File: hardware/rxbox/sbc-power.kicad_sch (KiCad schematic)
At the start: 41 parts, among them U2 SY8088, U3 SY8088, U4 SY8088, U5 SY8088, U6 ME6211C18M5, U7 SY8088

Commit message: supervisor + symbol, new journal. jumper for t113 power
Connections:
- net +5V renamed T113_5V
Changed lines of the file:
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@@
 		(in_pos_files yes)
 		(dnp no)
-		(fields_autoplaced yes)
 		(property "Reference" "#PWR07"
 			(at 52.07 91.44 0)
@@
 			)
 		)
-		(property "Value" "+5V"
-			(at 52.07 82.55 0)
+		(property "Value" "T113_5V"
+			(at 48.26 83.312 0)
 			(show_name no)
 			(do_not_autoplace no)
@@
 					(size 1.27 1.27)
 				)
+				(justify left)
 			)
 		)
@@
 		(in_pos_files yes)
 		(dnp no)
-		(fields_autoplaced yes)
 		(property "Reference" "#PWR016"
 			(at 140.97 91.44 0)
@@
 			)
 		)
-		(property "Value" "+5V"
-			(at 140.97 82.55 0)
+		(property "Value" "T113_5V"
+			(at 137.16 83.312 0)
 			(show_name no)
 			(do_not_autoplace no)
@@
 					(size 1.27 1.27)
 				)
+				(justify left)
 			)
 		)
@@
 		(in_pos_files yes)
 		(dnp no)
-		(fields_autoplaced yes)
 		(property "Reference" "#PWR02"
 			(at 53.34 50.8 0)
@@
 			)
 		)
-		(property "Value" "+5V"
-			(at 53.34 41.91 0)
+		(property "Value" "T113_5V"
+			(at 49.53 42.672 0)
 			(show_name no)
 			(do_not_autoplace no)
@@
 					(size 1.27 1.27)
 				)
+				(justify left)
 			)
 		)
@@
 			)
 		)
-		(property "Value" "+5V"
+		(property "Value" "T113_5V"
 			(at 52.07 123.19 0)
 			(show_name no)
@@
 		(in_pos_files yes)
 		(dnp no)
-		(fields_autoplaced yes)
 		(property "Reference" "#PWR03"
 			(at 143.51 46.99 0)
@@
 			)
 		)
-		(property "Value" "+5V"
-			(at 143.51 38.1 0)
+		(property "Value" "T113_5V"
+			(at 139.7 38.862 0)
 			(show_name no)
 			(do_not_autoplace no)
@@
 					(size 1.27 1.27)
 				)
+				(justify left)
 			)
 		)
@@
 			)
 		)
-		(property "Value" "+5V"
+		(property "Value" "T113_5V"
 			(at 226.06 82.55 0)
 			(show_name no)

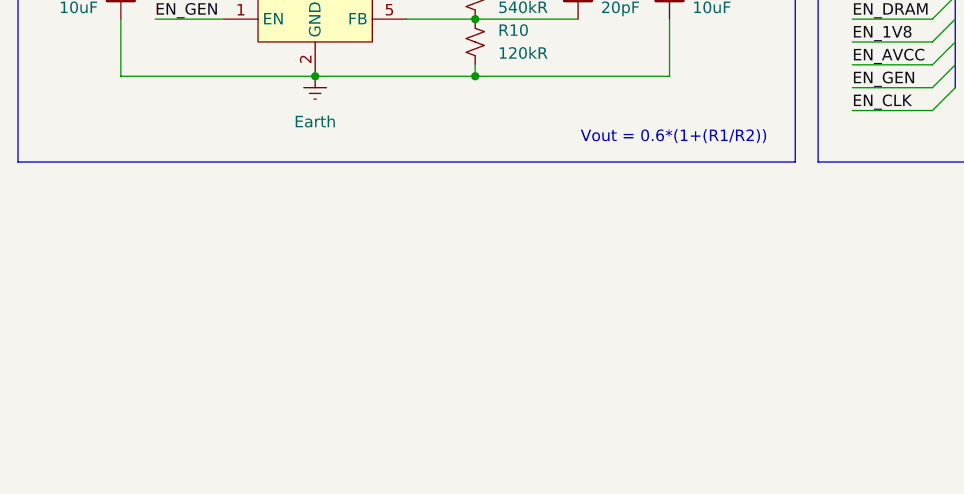
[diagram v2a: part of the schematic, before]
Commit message: wifi updates
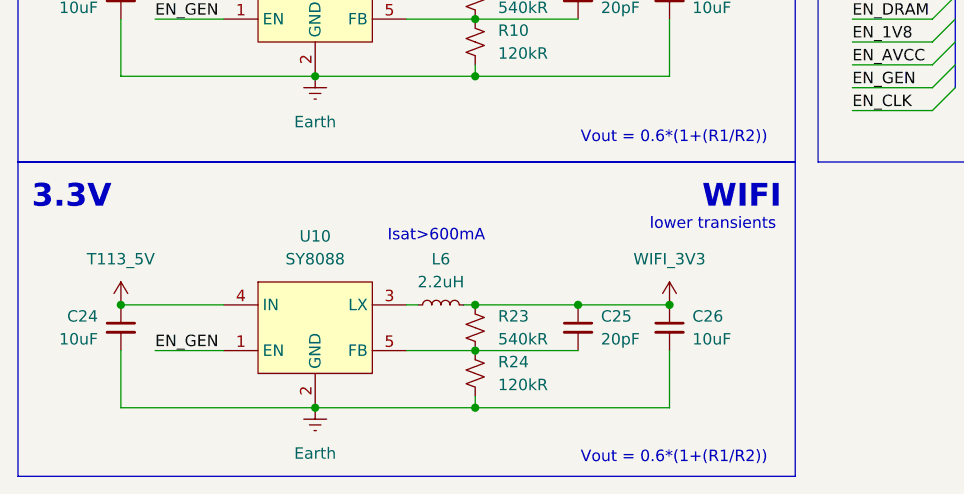
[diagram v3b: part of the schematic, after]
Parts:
- added C24, C26: 10uF, Capacitor_SMD:C_0402_1005Metric, symbol Device:C_Small
- added C25: 20pF, Capacitor_SMD:C_0402_1005Metric, symbol Device:C_Small
- added L6: 2.2uH, symbol Device:L_Small
- added R23: 540kR, Resistor_SMD:R_0402_1005Metric, symbol Device:R_Small_US
- added R24: 120kR, Resistor_SMD:R_0402_1005Metric, symbol Device:R_Small_US
- added U10: SY8088, Package_TO_SOT_SMD:SOT-23-5, symbol Regulator_Custom:SY8088
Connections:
- net EN_GEN: now also U10.1 (EN)
- net Earth: now also C24.2, C26.2, R24.2, U10.2 (GND)
- net T113_5V: now also C24.1, U10.4 (IN)
- new net: C25.2, R23.2, R24.1, U10.5 (FB)
- new net: L6.1, U10.3 (LX)
- new net WIFI_3V3: C25.1, C26.1, L6.2, R23.1
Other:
- note added: "WIFI"
- note added: "lower transients"

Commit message: wiring wifi + bt to t113
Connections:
- net T113_5V: no longer C24.1, U10.4 (IN)
- new net WIFI_5V: C24.1, U10.4 (IN)
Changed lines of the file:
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@@
 		(in_pos_files yes)
 		(dnp no)
-		(fields_autoplaced yes)
 		(property "Reference" "#PWR050"
 			(at 52.07 168.91 0)
@@
 			)
 		)
-		(property "Value" "T113_5V"
-			(at 52.07 160.02 0)
+		(property "Value" "WIFI_5V"
+			(at 53.34 163.83 0)
 			(show_name no)
 			(do_not_autoplace no)
@@
 					(size 1.27 1.27)
 				)
+				(justify left)
 			)
 		)

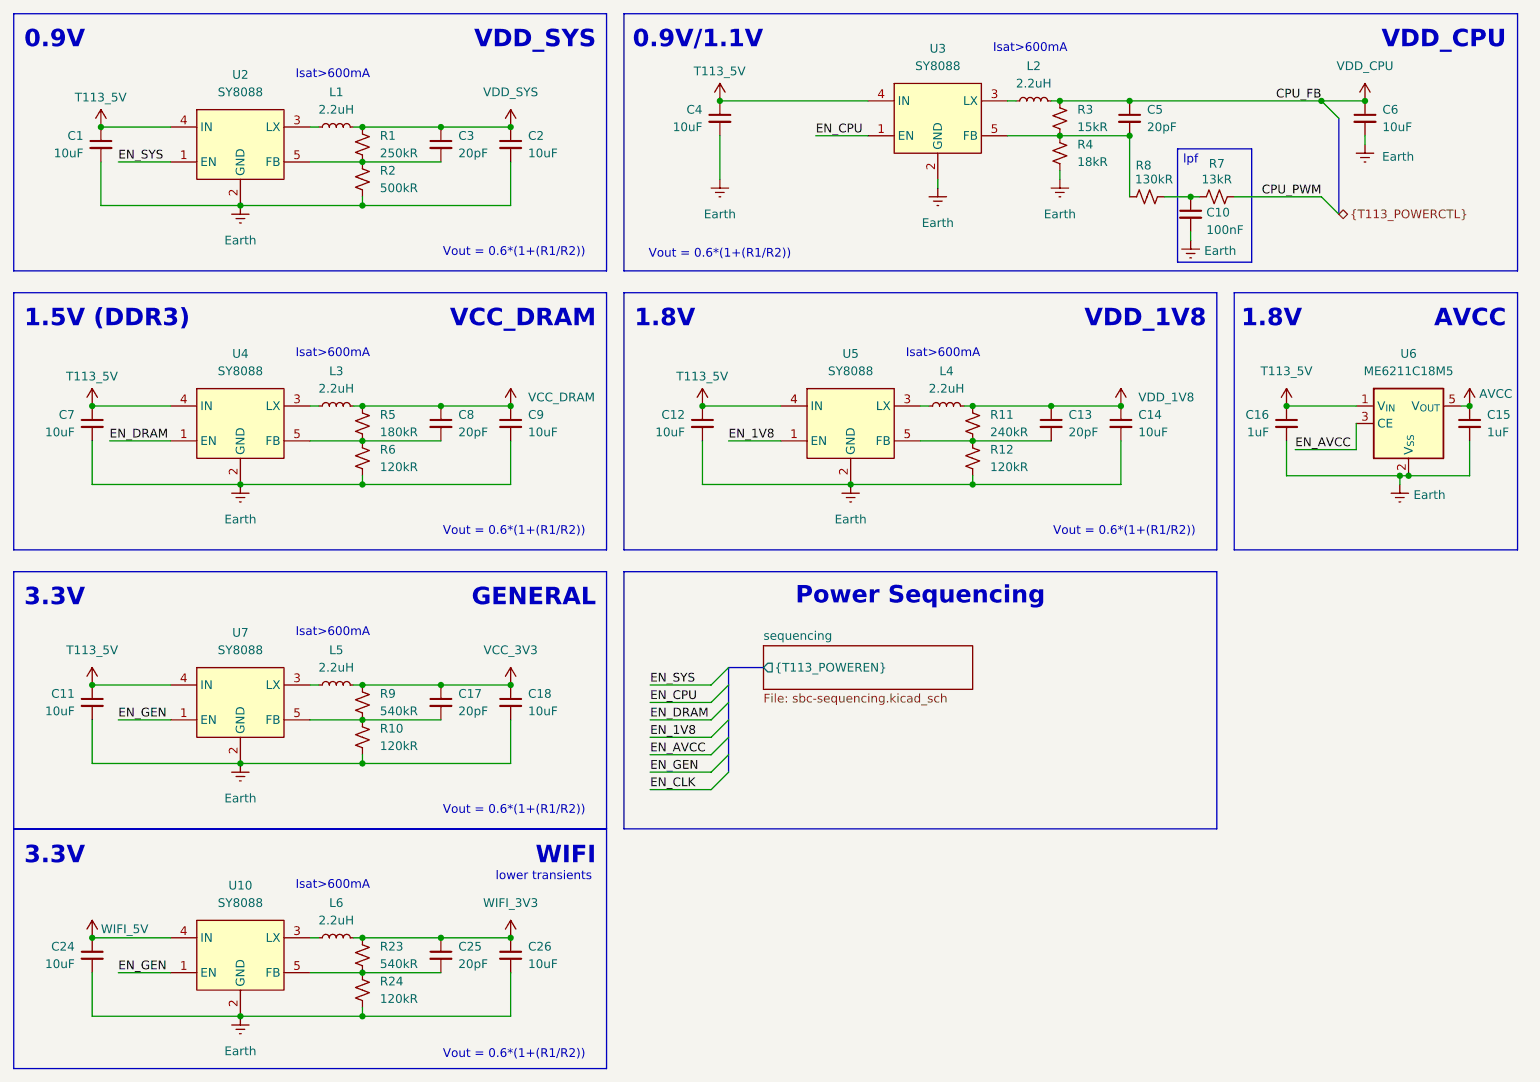
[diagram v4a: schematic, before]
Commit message: finish hooking up wifi+bt, and power
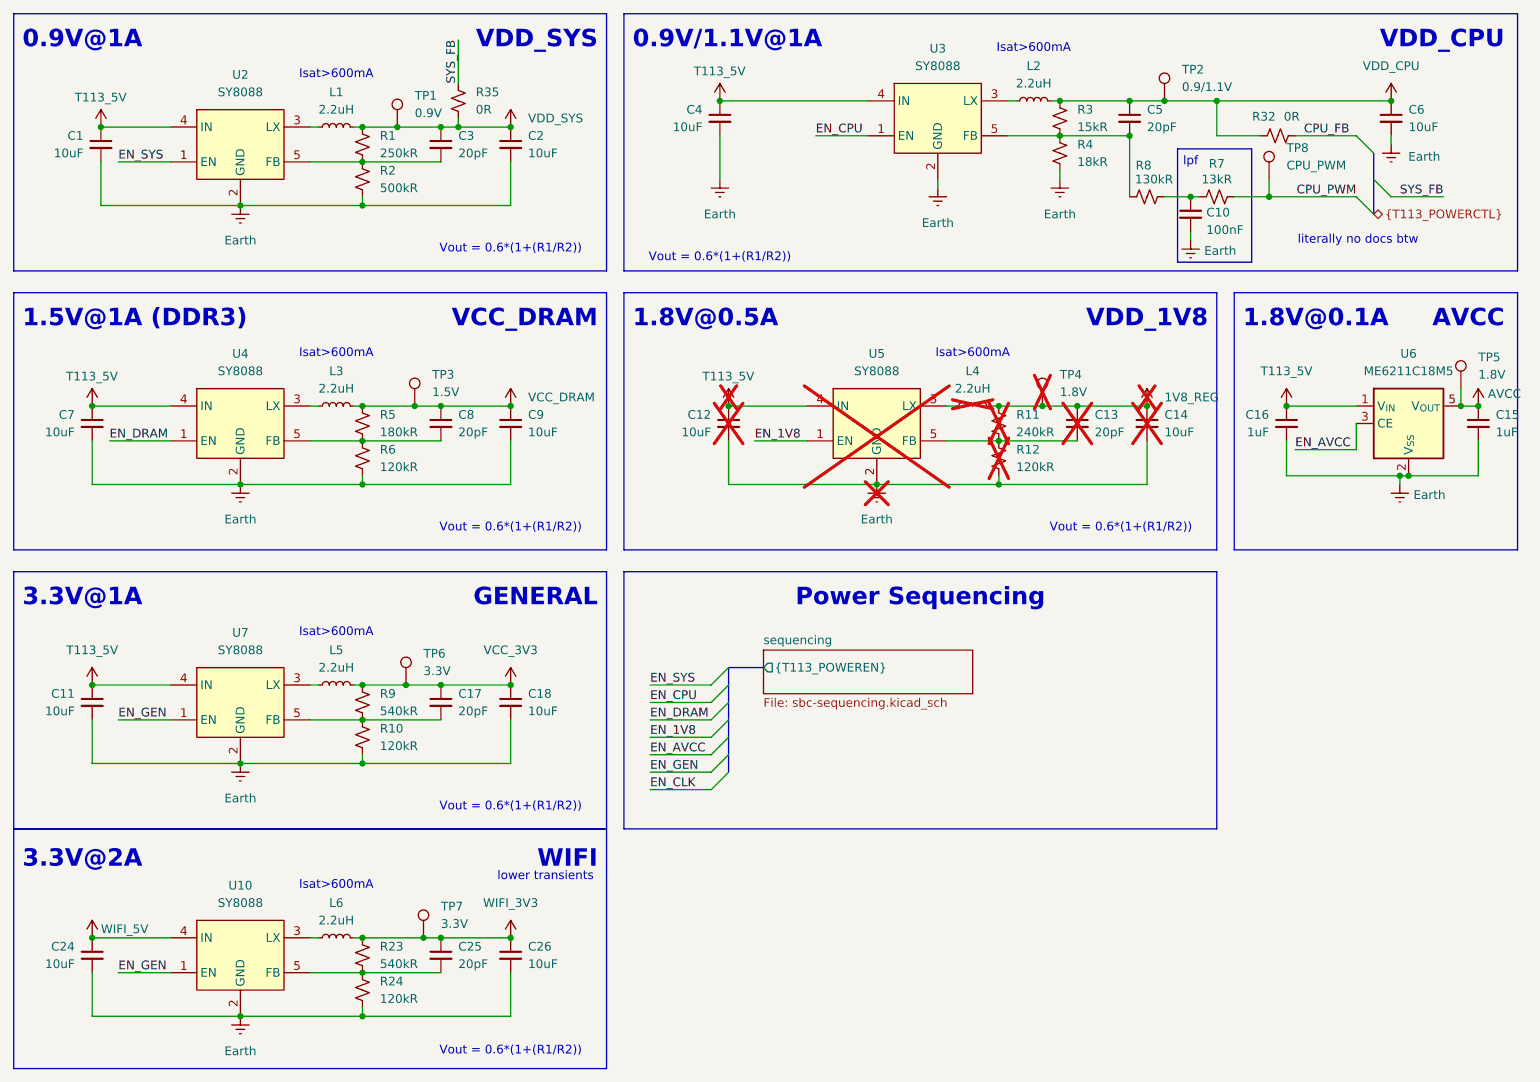
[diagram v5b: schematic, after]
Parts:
- added R32, R35: 0R, Resistor_SMD:R_0402_1005Metric, symbol Device:R_Small_US
- added TP1: 0.9V, TestPoint:TestPoint_Pad_D1.0mm, symbol Connector:TestPoint
- added TP2: 0.9/1.1V, TestPoint:TestPoint_Pad_D1.0mm, symbol Connector:TestPoint
- added TP3: 1.5V, TestPoint:TestPoint_Pad_D1.0mm, symbol Connector:TestPoint
- added TP4, TP5: 1.8V, TestPoint:TestPoint_Pad_D1.0mm, symbol Connector:TestPoint
- added TP6, TP7: 3.3V, TestPoint:TestPoint_Pad_D1.0mm, symbol Connector:TestPoint
- added TP8: CPU_PWM, TestPoint:TestPoint_Pad_D1.0mm, symbol Connector:TestPoint
- C12, C13, C14, L4, R11, R12, U5: now not fitted
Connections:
- net AVCC: now also TP5.1
- net CPU_PWM: now also TP8.1
- net VCC_3V3: now also TP6.1
- net VCC_DRAM: now also TP3.1
- net VDD_CPU: now also R32.1, TP2.1
- net VDD_SYS: now also R35.1, TP1.1
- net WIFI_3V3: now also TP7.1
- net VDD_1V8 renamed 1V8_REG
- net 1V8_REG: now also TP4.1
- new net CPU_FB: R32.2
- new net SYS_FB: R35.2
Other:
- note added: "0.9V/1.1V@1A"
- note added: "0.9V@1A"
- note added: "1.5V@1A (DDR3)"
- note added: "1.8V@0.1A"
- note added: "1.8V@0.5A"
- note added: "3.3V@1A"
- note added: "3.3V@2A"
- note added: "literally no docs btw"
- note removed: "0.9V"
- note removed: "0.9V/1.1V"
- note removed: "1.5V (DDR3)"
- note removed: "1.8V"
- note removed: "3.3V"
- moved on the sheet: C15, C6
